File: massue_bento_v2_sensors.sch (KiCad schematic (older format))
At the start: 18 parts, among them U6 AT42QT1070, U7 MPU9150, U8 MPL3115A2

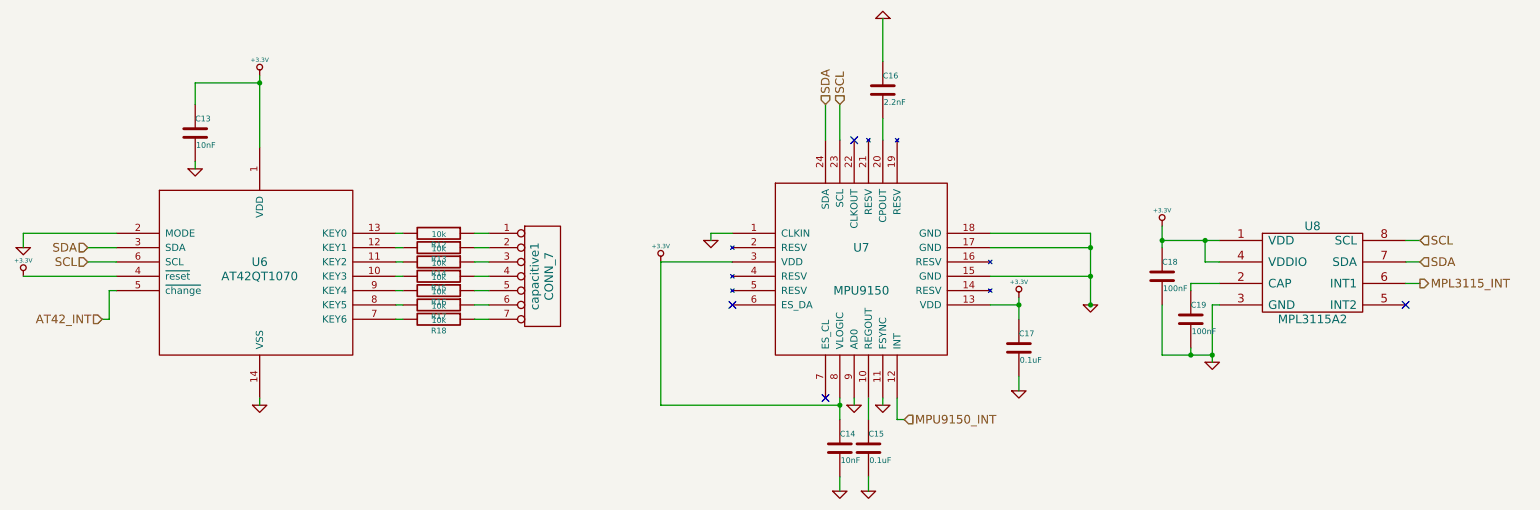
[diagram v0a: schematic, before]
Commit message: Clean: same value for 100nF/0.1uf capacitors, re-organization of labels, add dimension labels
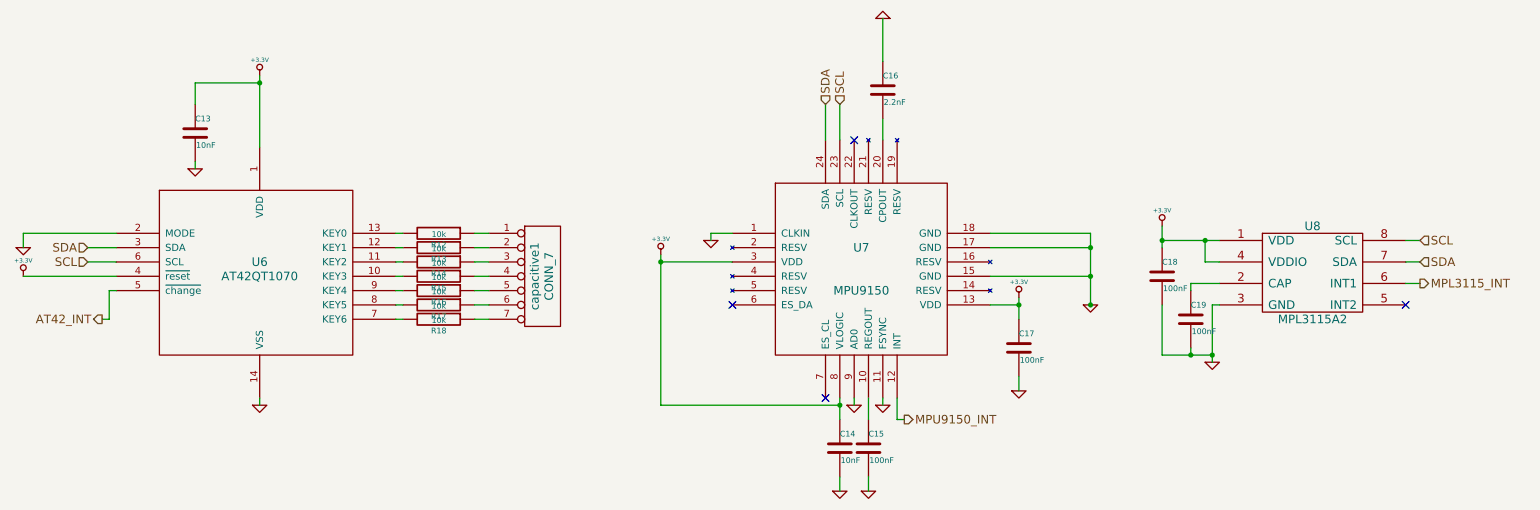
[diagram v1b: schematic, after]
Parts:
- C15, C17: value 0.1uF -> 100nF
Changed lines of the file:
@@
 L +3.3V #PWR042
 U 1 1 53A57777
-P 5200 4200
-F 0 "#PWR042" H 5200 4160 30  0001 C CNN
-F 1 "+3.3V" H 5200 4310 30  0000 C CNN
-F 2 "" H 5200 4200 60  0000 C CNN
-F 3 "" H 5200 4200 60  0000 C CNN
-	1    5200 4200
+P 5200 4150
+F 0 "#PWR042" H 5200 4110 30  0001 C CNN
+F 1 "+3.3V" H 5200 4260 30  0000 C CNN
+F 2 "" H 5200 4150 60  0000 C CNN
+F 3 "" H 5200 4150 60  0000 C CNN
+	1    5200 4150
 	1    0    0    -1
 $EndComp
@@
 P 7700 4800
 F 0 "C17" H 7700 4900 40  0000 L CNN
-F 1 "0.1uF" H 7706 4715 40  0000 L CNN
+F 1 "100nF" H 7706 4715 40  0000 L CNN
 F 2 "" H 7738 4650 30  0000 C CNN
 F 3 "" H 7700 4800 60  0000 C CNN
@@
 P 6650 5500
 F 0 "C15" H 6650 5600 40  0000 L CNN
-F 1 "0.1uF" H 6656 5415 40  0000 L CNN
+F 1 "100nF" H 6656 5415 40  0000 L CNN
 F 2 "" H 6688 5350 30  0000 C CNN
 F 3 "" H 6650 5500 60  0000 C CNN
@@
 	1    0    0    -1
 $EndComp
-Text HLabel 6900 5300 2    60   Input ~ 0
+Text HLabel 6900 5300 2    60   Output ~ 0
 MPU9150_INT
 $Comp
@@
 Connection ~ 6450 5200
 Wire Wire Line
-	5200 5200 5200 4200
-Wire Wire Line
-	6450 5200 5200 5200
+	5200 4150 5200 5200
+Wire Wire Line
+	5200 5200 6450 5200
 Wire Wire Line
 	6750 2500 6750 2800
@@
 Wire Wire Line
 	1950 3500 1950 3550
-Text HLabel 1300 4600 0    60   Input ~ 0
+Text HLabel 1300 4600 0    60   Output ~ 0
 AT42_INT
 Wire Wire Line
@@
 Wire Wire Line
 	10400 4350 10500 4350
+Connection ~ 5200 4200
 $EndSCHEMATC
